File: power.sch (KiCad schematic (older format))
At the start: 58 parts, among them J11 Conn_01x03, J12 Conn_01x01_Male, J13 Conn_01x02, J5 Conn_01x02, Q2 TSM085P03CV RGG, Q3 Q_NMOS_GSD, U7 MP2636GR-P, U8 NCP133AMX150TCG

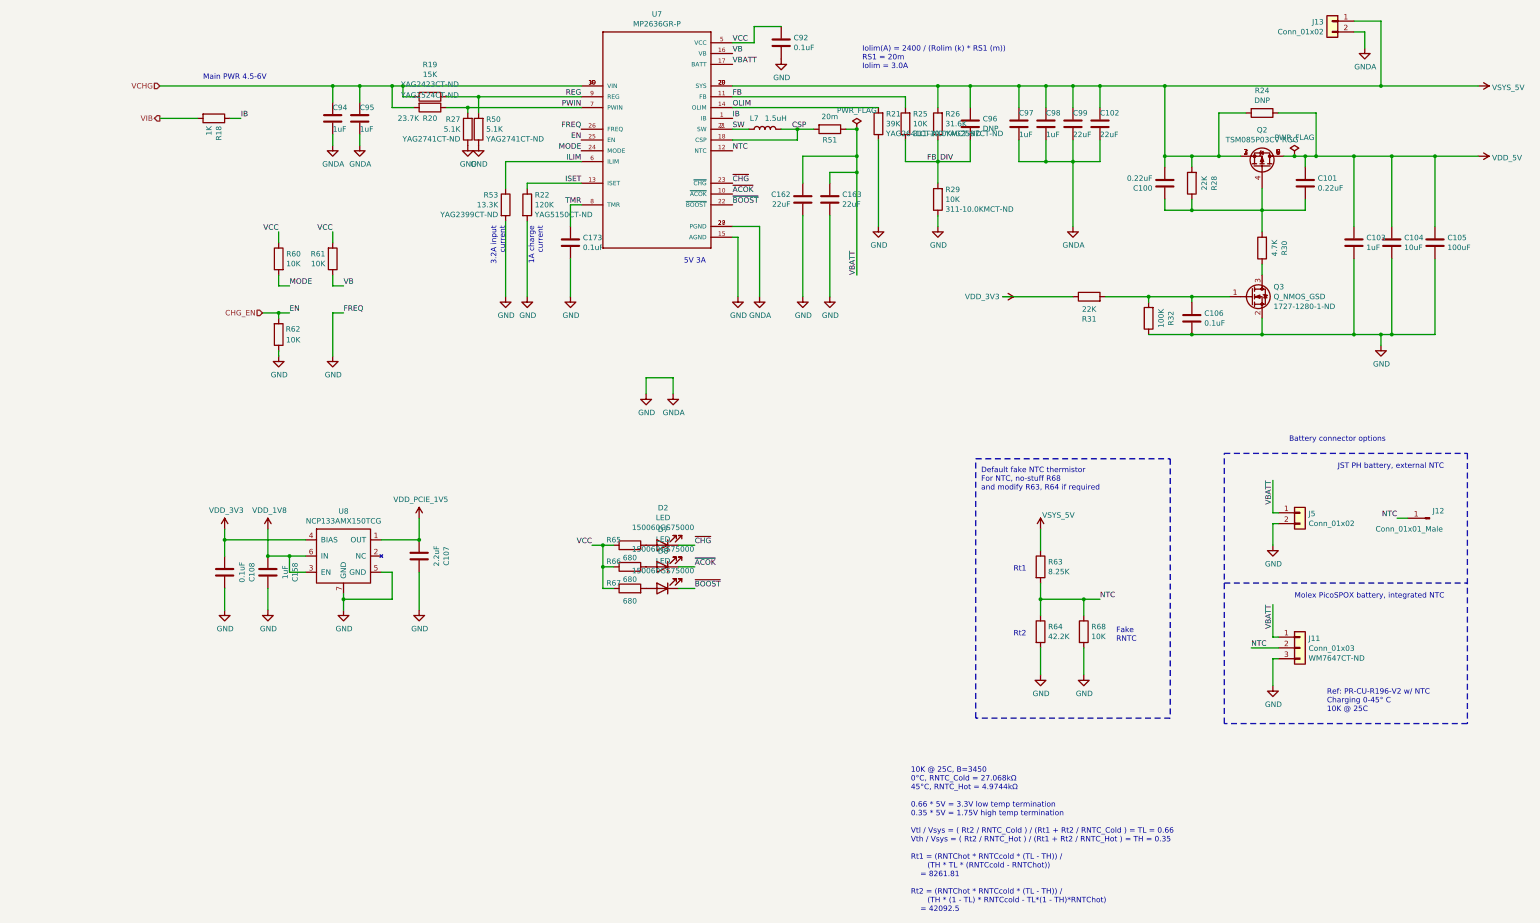
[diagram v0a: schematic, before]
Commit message: Re-annotate schematics, add dnp field, and silkscreen cleanup
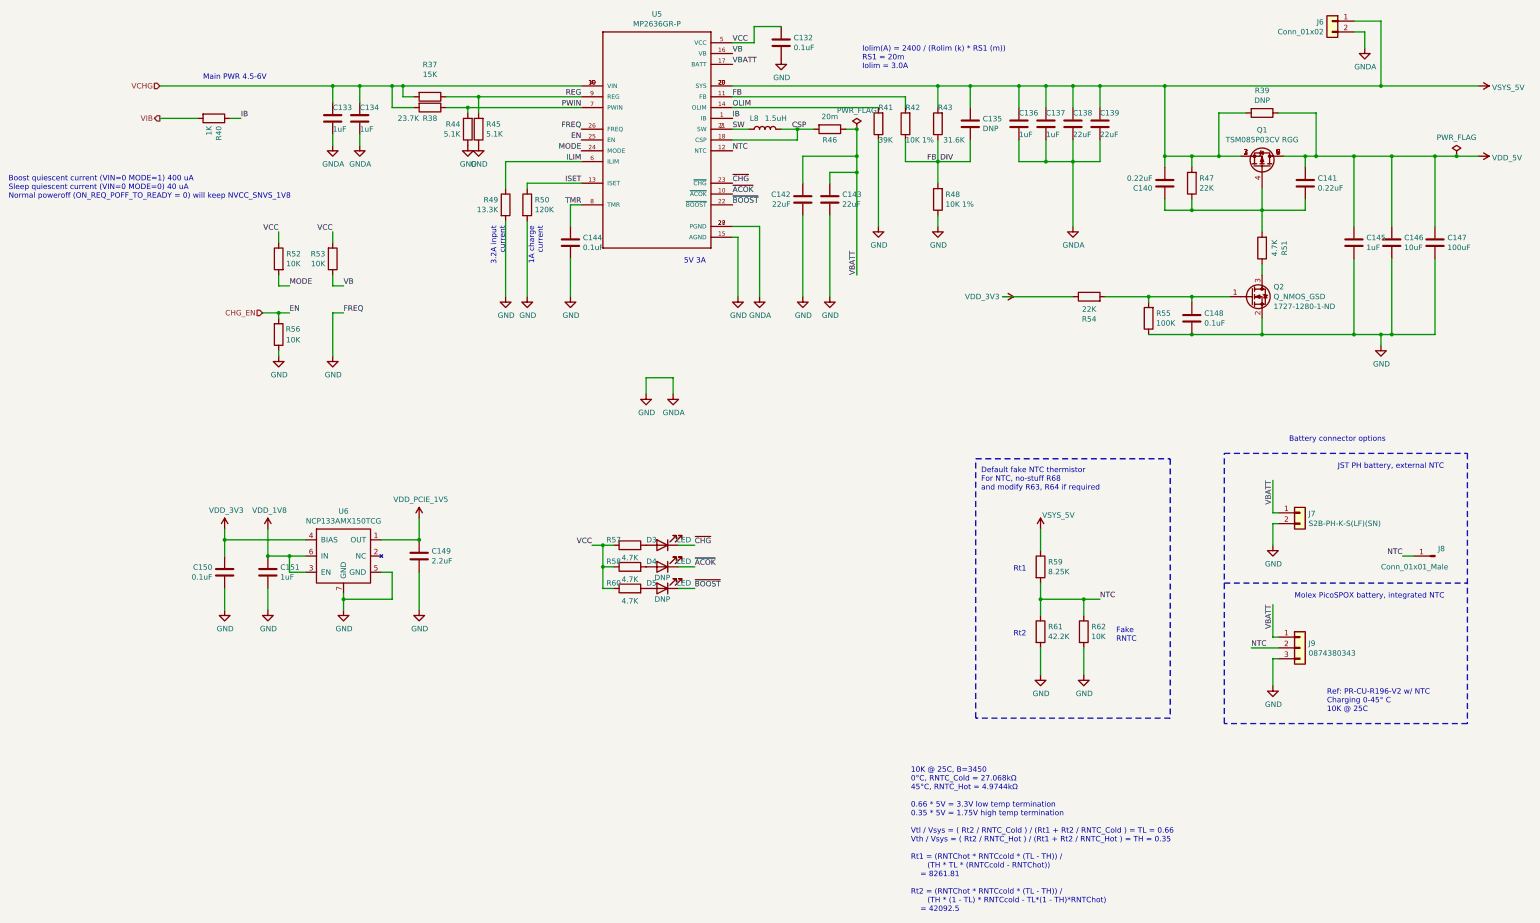
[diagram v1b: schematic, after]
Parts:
- C135: renamed from C96; Populate (none) -> DNP
- D4: renamed from D7; Populate (none) -> DNP
- D5: renamed from D8; Populate (none) -> DNP
- J6: renamed from J13; Populate (none) -> DNP
- J7: renamed from J5; value Conn_01x02 -> S2B-PH-K-S(LF)(SN)
- J8: renamed from J12; Populate (none) -> DNP
- J9: renamed from J11; value Conn_01x03 -> 0874380343; Populate (none) -> DNP
- R39: renamed from R24; Populate (none) -> DNP
- R42: renamed from R25; value 10K -> 10K 1%
- R48: renamed from R29; value 10K -> 10K 1%
- R57: renamed from R65; value 680 -> 4.7K; Part RC0201JR-07680RL -> RC0201JR-074K7L; Vendorpart 311-680NCT-ND -> 311-4.7KNCT-ND
- R58: renamed from R66; value 680 -> 4.7K; Part RC0201JR-07680RL -> RC0201JR-074K7L; Vendorpart 311-680NCT-ND -> 311-4.7KNCT-ND
- R60: renamed from R67; value 680 -> 4.7K; Part RC0201JR-07680RL -> RC0201JR-074K7L; Vendorpart 311-680NCT-ND -> 311-4.7KNCT-ND
- U5: renamed from U7; Field4 1.02 -> (none); Field5 Manufacturer Recommendation -> (none); Mfgr (none) -> Monolithic Power; Part (none) -> MP2636GR-Z; Vendorpart (none) -> 1589-1616-1-ND
- renumbered C92 to C132, C94 to C133, C95 to C134, C97 to C136, C98 to C137, C99 to C138, C102 to C139, C100 to C140, C101 to C141, C162 to C142, C163 to C143, C173 to C144, C103 to C145, C104 to C146, C105 to C147, C106 to C148, C107 to C149, C108 to C150, C158 to C151, D2 to D3, L7 to L8, Q2 to Q1, Q3 to Q2, R19 to R37, R20 to R38, R18 to R40, R21 to R41, R26 to R43, R27 to R44, R50 to R45, R51 to R46, R28 to R47, R53 to R49, R22 to R50, R30 to R51, R60 to R52, R61 to R53, R31 to R54, R32 to R55, R62 to R56, R63 to R59, R64 to R61, R68 to R62, U8 to U6
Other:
- note added: "Boost quiescent current (VIN=0 MODE=1) 400 uA\nSleep quiescent current (VIN=0 MODE=0) 40 uA\nNormal poweroff (ON_REQ_POFF_TO_READY = 0) will keep NVCC_SNVS_1V8"
- moved on the sheet: J8

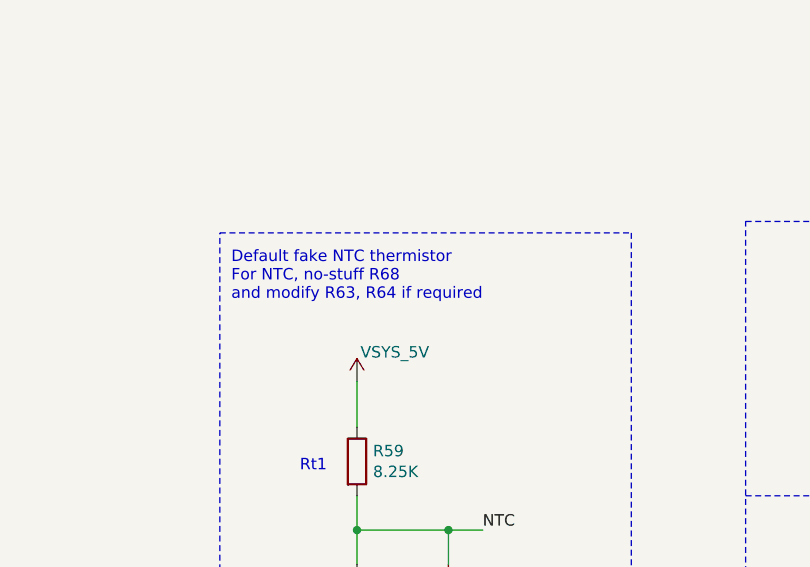
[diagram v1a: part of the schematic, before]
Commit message: Fixed a few comments related to component reference and make sure we're displaying dnp
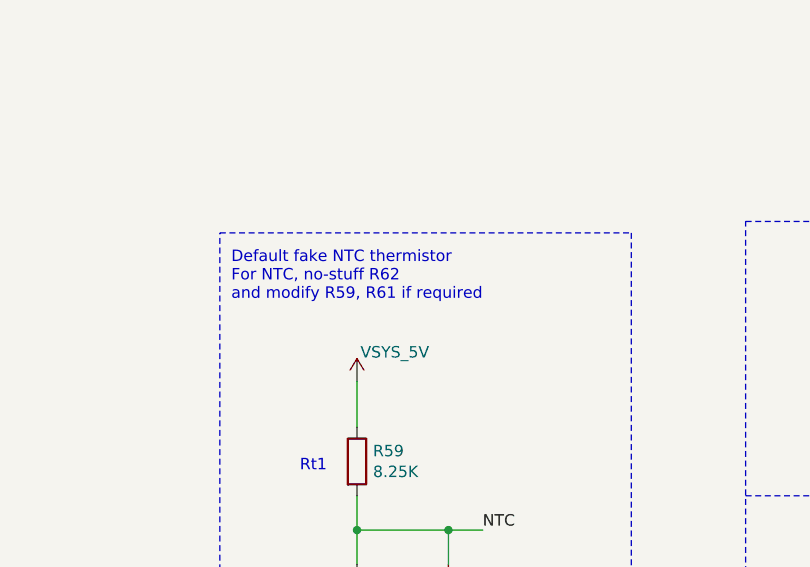
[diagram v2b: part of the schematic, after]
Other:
- note added: "Default fake NTC thermistor\nFor NTC, no-stuff R62\nand modify R59, R61 if required"
- note removed: "Default fake NTC thermistor\nFor NTC, no-stuff R68\nand modify R63, R64 if required"
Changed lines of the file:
@@
 	9500 5850 11300 5850
 Text Notes 9550 6150 0    50   ~ 0
-Default fake NTC thermistor\nFor NTC, no-stuff R68\nand modify R63, R64 if required
+Default fake NTC thermistor\nFor NTC, no-stuff R62\nand modify R59, R61 if required
 Text Notes 9850 6900 0    50   ~ 0
 Rt1

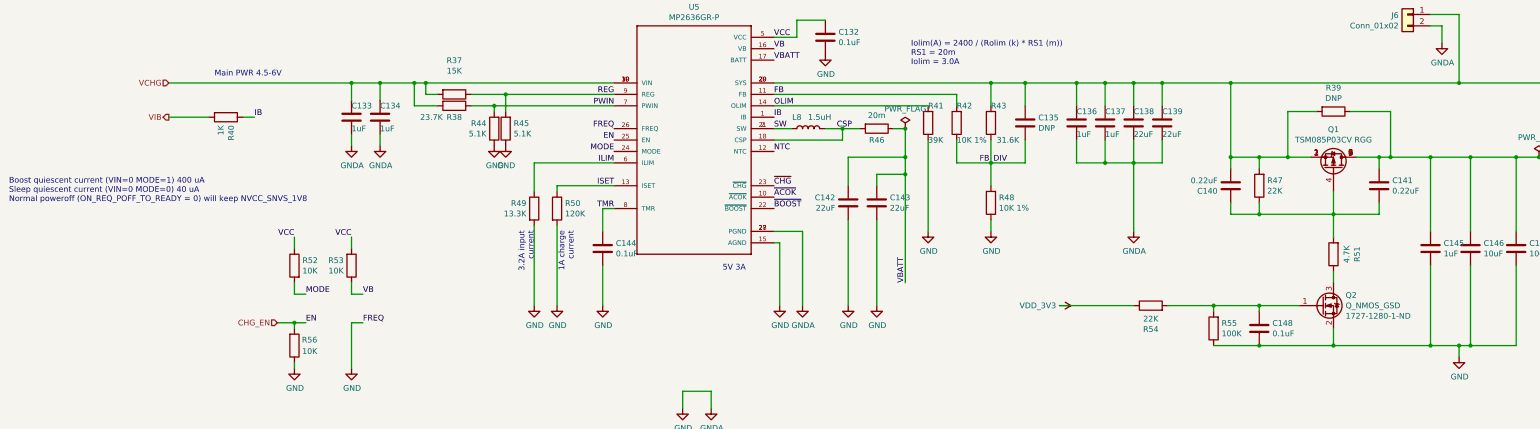
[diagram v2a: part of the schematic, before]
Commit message: Simplify control of VDD_5V with load switch
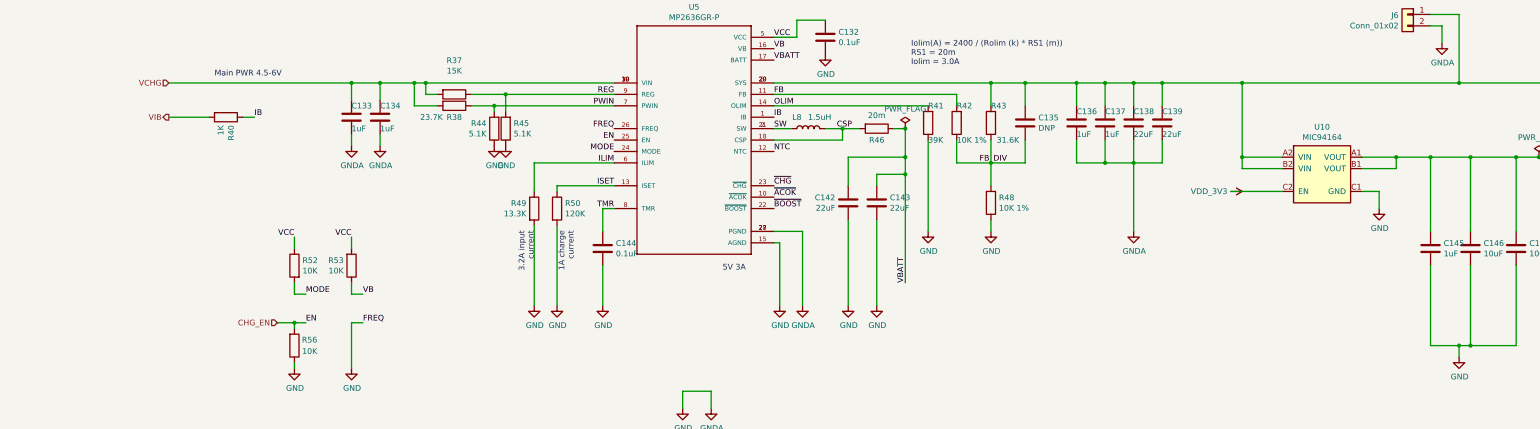
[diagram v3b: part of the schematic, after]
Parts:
- removed C140, C141: 0.22uF, Capacitor_SMD:C_0402_1005Metric, symbol Device:C
- removed C148: 0.1uF, Capacitor_SMD:C_0402_1005Metric, symbol Device:C
- removed Q1: TSM085P03CV RGG, Package_DFN_QFN:DFN-8-1EP_3x3mm_P0.65mm_EP1.55x2.4mm, symbol mxenc:AON7405
- removed Q2: Q_NMOS_GSD, Package_TO_SOT_SMD:SOT-323_SC-70, symbol Device:Q_NMOS_GSD
- removed R39: DNP, Resistor_SMD:R_0402_1005Metric, symbol Device:R
- removed R47, R54: 22K, Resistor_SMD:R_0402_1005Metric, symbol Device:R
- removed R51: 4.7K, Resistor_SMD:R_0402_1005Metric, symbol Device:R
- removed R55: 100K, Resistor_SMD:R_0402_1005Metric, symbol Device:R
- added U10: MIC94164, mxenc:BGA-6_3x2_1.5x1.0mm, symbol mxenc:MIC94164
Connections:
- net GND: now also U10.C1 (GND)
- net VDD_3V3: now also U10.C2 (EN)
- net VDD_5V: now also U10.A1 (VOUT), U10.B1 (VOUT)
- net VSYS_5V: now also U10.A2 (VIN), U10.B2 (VIN)
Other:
- note removed: "Boost quiescent current (VIN=0 MODE=1) 400 uA\nSleep quiescent current (VIN=0 MODE=0) 40 uA\nNormal poweroff (ON_REQ_POFF_TO_READY = 0) will keep NVCC_SNVS_1V8"
